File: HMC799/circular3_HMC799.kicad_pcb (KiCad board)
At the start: 2 copper layers, 25 x 25 mm, 37 parts, among them J101 Conn_Coaxial, J102 Conn_01x03, U101 LT3042xMSE, U102 LT3094xMSE, U103 HMC799LP3E, U104 BUF602xDBV

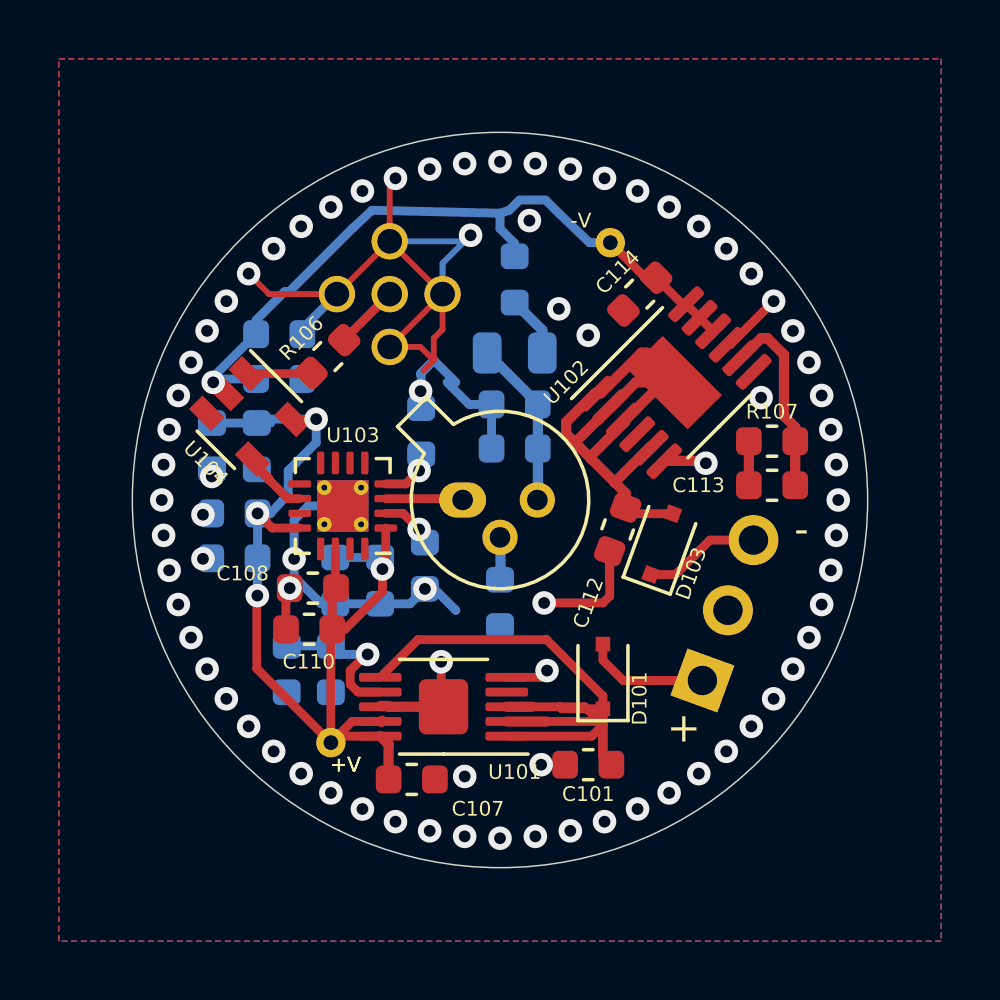
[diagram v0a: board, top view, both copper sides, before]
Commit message: ac-coupled, single-supply
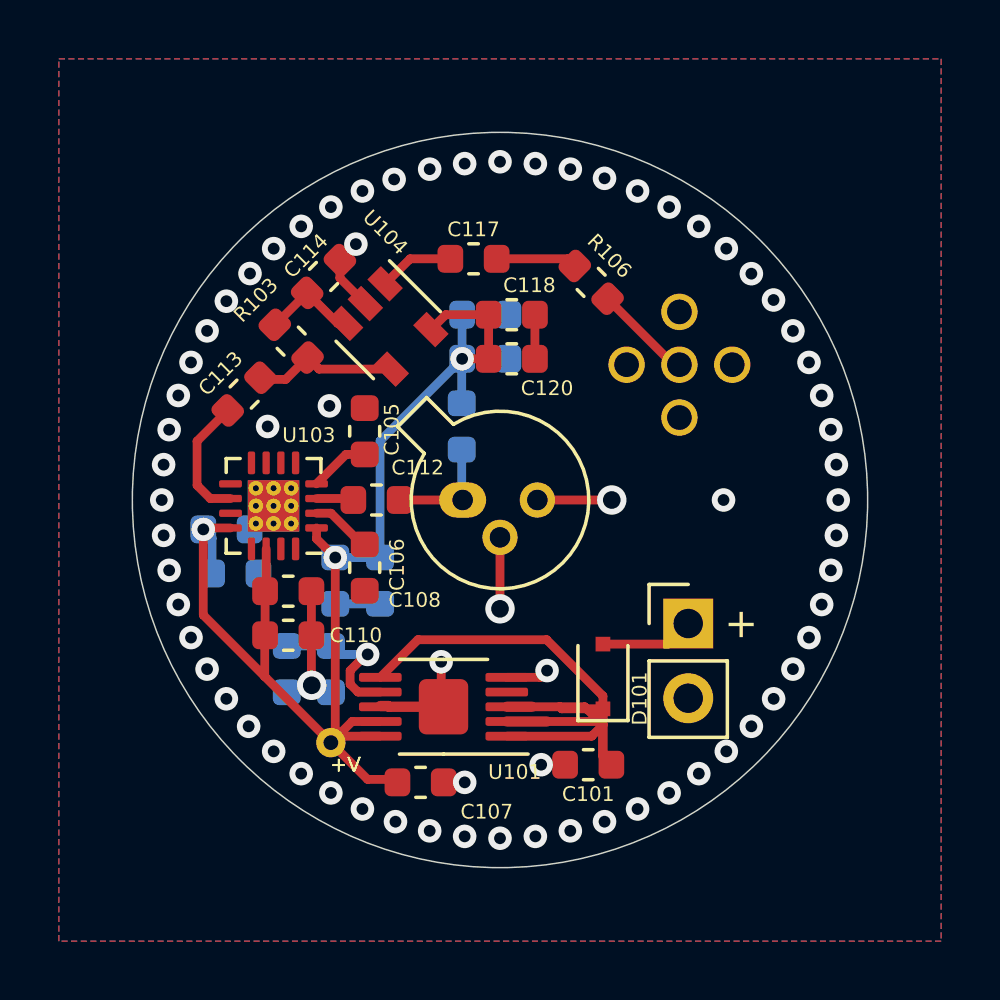
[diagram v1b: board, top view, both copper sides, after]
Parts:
- removed C119: 4u7, Capacitor_SMD:C_0603_1608Metric
- removed C121: 100n, Capacitor_SMD:C_0603_1608Metric
- removed D103: D, Diode_SMD:D_SOD-323F
- removed L101: 100u, Inductor_SMD:L_0805_2012Metric
- removed R107: 25k, Resistor_SMD:R_0603_1608Metric
- removed TP101: TestPoint, TestPoint:TestPoint_THTPad_D1.0mm_Drill0.5mm
- removed U102: LT3094xMSE, Package_SO:MSOP-12-1EP_3x4mm_P0.65mm_EP1.65x2.85mm
- added C117: 100n, Capacitor_SMD:C_0603_1608Metric, F.Cu at (149.1, 91.8)
- C105, C106, C118, C120: moved to F.Cu
- C112, C113: value 4u7 -> 22n
- C114: value 4u7 -> 100n
- J102: value Conn_01x03 -> Conn_01x02; footprint Connector_PinHeader_2.54mm:PinHeader_1x03_P2.54mm_Vertical -> Connector_PinHeader_2.54mm:PinHeader_1x02_P2.54mm_Vertical; moved to F.Cu
- R102: value 300R -> 10k
- R103: value 0R -> 2k; moved to F.Cu
- U103: footprint Package_DFN_QFN:QFN-16-1EP_3x3mm_P0.5mm_EP1.75x1.75mm_ThermalVias -> awallinKiCadFootprints:QFN-16-1EP_3x3mm_P0.5mm_EP1.75x1.75mm_ThermalVias9
- moved C113 18.2 mm to (141.3, 96.4), turned to 225 degrees
- moved R103 11.4 mm to (142.9, 94.6), turned to 135 degrees
- moved C114 10.8 mm to (144.0, 92.4)
- moved C120 10.6 mm to (150.4, 95.2), turned to 180 degrees
- moved J101 10.1 mm to (156.1, 95.4), turned to 45 degrees
- moved C118 9.75 mm to (150.4, 93.7), turned to 180 degrees
- moved R106 9.30 mm to (153.1, 92.6), turned to 135 degrees
- moved C112 8.26 mm to (145.8, 100.0), turned to 0 degrees
- moved U104 5.62 mm to (146.2, 94.1)
- moved R102 5.31 mm to (148.7, 97.5)
- moved C104 4.66 mm to (149.5, 93.7), turned to 0 degrees
- moved U103 2.35 mm to (142.3, 100.2)
- moved C106 2.05 mm to (145.4, 102.3)
- moved J102 2.00 mm to (156.4, 104.2), turned to 0 degrees
- moved C105 1.92 mm to (145.4, 97.7)
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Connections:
- C102 pad 1: /VBIAS -> /+V
- C104 pad 1: /VBIAS -> /+V
- C112 pad 1: GND -> Net-(C112-Pad1)
- C113 pad 1: GND -> Net-(C113-Pad1)
- C113 pad 2: /SET- -> Net-(C113-Pad2)
- C114 pad 1: GND -> Net-(C114-Pad1)
- C114 pad 2: /-V -> GND
- D102 pad 1: /PD -> Net-(C112-Pad2)
- D102 pad 2: Net-(D102-Pad2) -> GND
- D102 pad 3: /VBIAS -> GND
- R102 pad 1: /-V -> /+V
- R102 pad 2: Net-(L101-Pad1) -> Net-(C112-Pad2)
- R103 pad 1: GND -> Net-(C113-Pad1)
- R103 pad 2: Net-(D102-Pad2) -> Net-(C114-Pad1)
- R106 pad 2: Net-(R106-Pad2) -> Net-(C117-Pad1)
- U103 pad 10: Net-(U103-Pad10) -> Net-(C113-Pad2)
- U103 pad 3: /PD -> Net-(C112-Pad1)
- U104 pad 1: Net-(R106-Pad2) -> Net-(C117-Pad2)
- U104 pad 2: /-V -> GND
- U104 pad 3: Net-(U104-Pad3) -> Net-(C114-Pad1)
- U104 pad 4: Net-(U103-Pad10) -> Net-(C113-Pad1)
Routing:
- net GND: track 59.0 -> 19.9 mm, vias 78 -> 71
- net /-V: track 25.6 -> 0.00 mm, vias 1 -> 0
- net Net-(C112-Pad2): track 20.9 -> 3.93 mm
- net /+V: track 37.7 -> 46.9 mm, vias 4 -> 3
- net /SET-: track 6.55 -> 0.00 mm
- net /VBIAS: track 5.72 -> 0.00 mm
- net Net-(C113-Pad1): track 0.00 -> 4.94 mm
- net /-VIN: track 4.71 -> 0.00 mm
- net Net-(C113-Pad2): track 0.00 -> 4.30 mm
- net Net-(C114-Pad1): track 0.00 -> 3.29 mm
- net Net-(D102-Pad2): track 2.94 -> 0.00 mm
- net Net-(C117-Pad1): track 0.00 -> 2.76 mm
- net /PD: track 2.63 -> 0.00 mm
- net Net-(C117-Pad2): track 0.00 -> 2.57 mm
- net Net-(U103-Pad10): track 2.54 -> 0.00 mm
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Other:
- board text added: "1" Fast Detector AW2020-05-27"
- board text added: "MAX +20V"
- board text removed: "-"
- board text removed: "-V"
- board text removed: "-V GND +V"
- board text removed: "1" Fast Detector AW2020-05-12"
- board text removed: "MAX +/-20V"

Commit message: 0402 caps
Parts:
- C105, C112, C113: footprint Capacitor_SMD:C_0603_1608Metric -> Capacitor_SMD:C_0402_1005Metric
- moved C105 0.42 mm to (145.0, 97.8)

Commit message: finalize for PCB order
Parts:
- added L101: L, Inductor_SMD:L_0805_2012Metric, B.Cu at (149.7, 91.9)
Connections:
- C102 pad 1: /+V -> Net-(C102-Pad1)
- C104 pad 1: /+V -> Net-(C102-Pad1)
- R102 pad 1: /+V -> Net-(C102-Pad1)
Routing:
- net Net-(C102-Pad1): track 0.00 -> 4.84 mm
- net /+V: track 46.9 -> 51.3 mm
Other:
- net class Default: clearance 0.15 -> 0.25
- rule trace_clearance: 0.15 -> 0.25
